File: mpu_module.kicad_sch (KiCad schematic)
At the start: 12 parts

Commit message: Eliminated all warnings realted with footprints
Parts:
- C55, C56: footprint Capacitors_Smd_0603:100nF_0603 -> Capacitors_Smd_0402:100nF_0402; symbol Capacitors_Smd0603:100n -> Capacitors_Smd0402:100nF; Developer (none) -> MW; LCSC Part # (optional) (none) -> C131394; Manufacturer SAMSUNG -> Murata; Manufacturer Part Number CL10B104JB8NNNC -> GRM155R71H104KE14D; Package 0603 -> 0402; Package_1 (none) -> 0402; Price@1000pcs 0,02231 -> 0,03299; Price@1pc 0,04540 -> 0,07091; Supplier TME -> Tme; Supplier Part Number CL10B104JB8NNNC -> GRM155R71H104KE14D; URL https://www.tme.eu/pl/details/cl10b104jb8nnnc/kondensatory-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 -> https://www.tme.eu/pl/details/grm155r71h104ke14d/kondensato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
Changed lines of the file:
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@@
     (pin "1")
   )
-  (symbol (lib_id "Capacitors_Smd0603:100n") (at 41.91 115.57 0) (unit 1)
+  (symbol (lib_id "Capacitors_Smd0402:100nF") (at 41.91 115.57 0) (unit 1)
     (in_bom yes) (on_board yes)
     (property "Reference" "C56" (id 0) (at 45.2374 114.4016 0)
@@
       (effects (font (size 1.27 1.27)) (justify left))
     )
-    (property "Footprint" "Capacitors_Smd_0603:100nF_0603" (id 2) (at 41.91 115.57 0)
-      (effects (font (size 1.524 1.524)) hide)
-    )
-    (property "Datasheet" "Capacitors/Smd_0603/Components_Documentation/KEM_C1005_Y5V_SMD.pdf" (id 3) (at 41.91 115.57 0)
-      (effects (font (size 1.524 1.524)) hide)
-    )
-    (property "Manufacturer" "SAMSUNG" (id 4) (at 41.91 115.57 0)
+    (property "Footprint" "Capacitors_Smd_0402:100nF_0402" (id 2) (at 41.91 115.57 0)
       (effects (font (size 1.27 1.27)) hide)
     )
-    (property "Manufacturer Part Number" "CL10B104JB8NNNC" (id 5) (at 41.91 115.57 0)
+    (property "Datasheet" "https://www.tme.eu/Document/558f361ed82994aff5a3e7789d970dd1/GRM155R71H104KE14-01.pdf" (id 3) (at 41.91 115.57 0)
       (effects (font (size 1.27 1.27)) hide)
     )
-    (property "Supplier" "TME" (id 6) (at 41.91 115.57 0)
+    (property "Manufacturer" "Murata" (id 4) (at 41.91 115.57 0)
       (effects (font (size 1.27 1.27)) hide)
     )
-    (property "Supplier Part Number" "CL10B104JB8NNNC" (id 7) (at 41.91 115.57 0)
+    (property "Manufacturer Part Number" "GRM155R71H104KE14D" (id 5) (at 41.91 115.57 0)
       (effects (font (size 1.27 1.27)) hide)
     )
-    (property "URL" "https://www.tme.eu/pl/details/cl10b104jb8nnnc/kondensatory-mlcc-smd-0603/samsung/" (id 8) (at 41.91 115.57 0)
+    (property "Supplier" "Tme" (id 6) (at 41.91 115.57 0)
       (effects (font (size 1.27 1.27)) hide)
     )
-    (property "Price@1pc" "0,04540" (id 9) (at 41.91 115.57 0)
+    (property "Supplier Part Number" "GRM155R71H104KE14D" (id 7) (at 41.91 115.57 0)
       (effects (font (size 1.27 1.27)) hide)
     )
-    (property "Price@1000pcs" "0,02231" (id 10) (at 41.91 115.57 0)
+    (property "URL" "https://www.tme.eu/pl/details/grm155r71h104ke14d/kondensatory-mlcc-smd-0402/murata/" (id 8) (at 41.91 115.57 0)
       (effects (font (size 1.27 1.27)) hide)
     )
-    (property "Package" "0603" (id 11) (at 41.91 115.57 0)
+    (property "Price@1pc" "0,07091" (id 9) (at 41.91 115.57 0)
+      (effects (font (size 1.27 1.27)) hide)
+    )
+    (property "Price@1000pcs" "0,03299" (id 10) (at 41.91 115.57 0)
+      (effects (font (size 1.27 1.27)) hide)
+    )
+    (property "Package" "0402" (id 11) (at 41.91 115.57 0)
+      (effects (font (size 1.27 1.27)) hide)
+    )
+    (property "Developer" "MW" (id 12) (at 41.91 115.57 0)
+      (effects (font (size 1.27 1.27)) hide)
+    )
+    (property "Package_1" "0402" (id 13) (at 41.91 115.57 0)
+      (effects (font (size 1.27 1.27)) hide)
+    )
+    (property "LCSC Part # (optional)" "C131394" (id 14) (at 41.91 115.57 0)
       (effects (font (size 1.27 1.27)) hide)
     )
@@
     (pin "1")
   )
-  (symbol (lib_id "Capacitors_Smd0603:100n") (at 29.21 115.57 0) (unit 1)
+  (symbol (lib_id "Capacitors_Smd0402:100nF") (at 29.21 115.57 0) (unit 1)
     (in_bom yes) (on_board yes)
     (property "Reference" "C55" (id 0) (at 32.5374 114.4016 0)
@@
       (effects (font (size 1.27 1.27)) (justify left))
     )
-    (property "Footprint" "Capacitors_Smd_0603:100nF_0603" (id 2) (at 29.21 115.57 0)
-      (effects (font (size 1.524 1.524)) hide)
-    )
-    (property "Datasheet" "Capacitors/Smd_0603/Components_Documentation/KEM_C1005_Y5V_SMD.pdf" (id 3) (at 29.21 115.57 0)
-      (effects (font (size 1.524 1.524)) hide)
-    )
-    (property "Manufacturer" "SAMSUNG" (id 4) (at 29.21 115.57 0)
+    (property "Footprint" "Capacitors_Smd_0402:100nF_0402" (id 2) (at 29.21 115.57 0)
       (effects (font (size 1.27 1.27)) hide)
     )
-    (property "Manufacturer Part Number" "CL10B104JB8NNNC" (id 5) (at 29.21 115.57 0)
+    (property "Datasheet" "https://www.tme.eu/Document/558f361ed82994aff5a3e7789d970dd1/GRM155R71H104KE14-01.pdf" (id 3) (at 29.21 115.57 0)
       (effects (font (size 1.27 1.27)) hide)
     )
-    (property "Supplier" "TME" (id 6) (at 29.21 115.57 0)
+    (property "Manufacturer" "Murata" (id 4) (at 29.21 115.57 0)
       (effects (font (size 1.27 1.27)) hide)
     )
-    (property "Supplier Part Number" "CL10B104JB8NNNC" (id 7) (at 29.21 115.57 0)
+    (property "Manufacturer Part Number" "GRM155R71H104KE14D" (id 5) (at 29.21 115.57 0)
       (effects (font (size 1.27 1.27)) hide)
     )
-    (property "URL" "https://www.tme.eu/pl/details/cl10b104jb8nnnc/kondensatory-mlcc-smd-0603/samsung/" (id 8) (at 29.21 115.57 0)
+    (property "Supplier" "Tme" (id 6) (at 29.21 115.57 0)
       (effects (font (size 1.27 1.27)) hide)
     )
-    (property "Price@1pc" "0,04540" (id 9) (at 29.21 115.57 0)
+    (property "Supplier Part Number" "GRM155R71H104KE14D" (id 7) (at 29.21 115.57 0)
       (effects (font (size 1.27 1.27)) hide)
     )
-    (property "Price@1000pcs" "0,02231" (id 10) (at 29.21 115.57 0)
+    (property "URL" "https://www.tme.eu/pl/details/grm155r71h104ke14d/kondensatory-mlcc-smd-0402/murata/" (id 8) (at 29.21 115.57 0)
       (effects (font (size 1.27 1.27)) hide)
     )
-    (property "Package" "0603" (id 11) (at 29.21 115.57 0)
+    (property "Price@1pc" "0,07091" (id 9) (at 29.21 115.57 0)
       (effects (font (size 1.27 1.27)) hide)
     )
+    (property "Price@1000pcs" "0,03299" (id 10) (at 29.21 115.57 0)
+      (effects (font (size 1.27 1.27)) hide)
+    )
+    (property "Package" "0402" (id 11) (at 29.21 115.57 0)
+      (effects (font (size 1.27 1.27)) hide)
+    )
+    (property "Developer" "MW" (id 12) (at 29.21 115.57 0)
+      (effects (font (size 1.27 1.27)) hide)
+    )
+    (property "Package_1" "0402" (id 13) (at 29.21 115.57 0)
+      (effects (font (size 1.27 1.27)) hide)
+    )
+    (property "LCSC Part # (optional)" "C131394" (id 14) (at 29.21 115.57 0)
+      (effects (font (size 1.27 1.27)) hide)
+    )

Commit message: Gerbers created, BOM, CPL
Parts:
- C55, C56: value 100n -> 100nF/50V
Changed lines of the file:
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@@
       (effects (font (size 1.27 1.27)) hide)
     )
-    (property "Datasheet" "Resistors/Smd_0603/Components_Documentation/Vishay_Resistors_SM0603.pdf" (id 3) (at 161.29 193.04 0)
+    (property "Datasheet" "https://www.tme.eu/Document/b315665a56acbc42df513c99b390ad98/ROYALOHM-THICKFILM.pdf" (id 3) (at 161.29 193.04 0)
       (effects (font (size 1.27 1.27)) hide)
     )
@@
       (effects (font (size 1.27 1.27)) hide)
     )
-    (property "Datasheet" "Resistors/Smd_0603/Components_Documentation/Vishay_Resistors_SM0603.pdf" (id 3) (at 144.78 130.81 0)
+    (property "Datasheet" "https://www.tme.eu/Document/b315665a56acbc42df513c99b390ad98/ROYALOHM-THICKFILM.pdf" (id 3) (at 144.78 130.81 0)
       (effects (font (size 1.27 1.27)) hide)
     )
@@
       (effects (font (size 1.524 1.524)) hide)
     )
-    (property "Datasheet" "Resistors/Smd_0603/Components_Documentation/Vishay_Resistors_SM0603.pdf" (id 3) (at 25.4 158.75 0)
+    (property "Datasheet" "https://www.tme.eu/Document/4f50d320a6ddacb273098f84373b6259/rezystor-smd.pdf" (id 3) (at 25.4 158.75 0)
       (effects (font (size 1.524 1.524)) hide)
     )
@@
       (effects (font (size 1.524 1.524)) hide)
     )
-    (property "Datasheet" "Resistors/Smd_0603/Components_Documentation/Vishay_Resistors_SM0603.pdf" (id 3) (at 33.02 158.75 0)
+    (property "Datasheet" "https://www.tme.eu/Document/4f50d320a6ddacb273098f84373b6259/rezystor-smd.pdf" (id 3) (at 33.02 158.75 0)
       (effects (font (size 1.524 1.524)) hide)
     )
@@
       (effects (font (size 1.524 1.524)) hide)
     )
-    (property "Datasheet" "Resistors/Smd_0603/Components_Documentation/Vishay_Resistors_SM0603.pdf" (id 3) (at 40.64 158.75 0)
+    (property "Datasheet" "https://www.tme.eu/Document/4f50d320a6ddacb273098f84373b6259/rezystor-smd.pdf" (id 3) (at 40.64 158.75 0)
       (effects (font (size 1.524 1.524)) hide)
     )
@@
       (effects (font (size 1.524 1.524)) hide)
     )
-    (property "Datasheet" "Resistors/Smd_0603/Components_Documentation/Vishay_Resistors_SM0603.pdf" (id 3) (at 25.4 181.61 0)
+    (property "Datasheet" "https://www.tme.eu/Document/4f50d320a6ddacb273098f84373b6259/rezystor-smd.pdf" (id 3) (at 25.4 181.61 0)
       (effects (font (size 1.524 1.524)) hide)
     )
@@
       (effects (font (size 1.524 1.524)) hide)
     )
-    (property "Datasheet" "Resistors/Smd_0603/Components_Documentation/Vishay_Resistors_SM0603.pdf" (id 3) (at 33.02 181.61 0)
+    (property "Datasheet" "https://www.tme.eu/Document/4f50d320a6ddacb273098f84373b6259/rezystor-smd.pdf" (id 3) (at 33.02 181.61 0)
       (effects (font (size 1.524 1.524)) hide)
     )
@@
       (effects (font (size 1.524 1.524)) hide)
     )
-    (property "Datasheet" "Resistors/Smd_0603/Components_Documentation/Vishay_Resistors_SM0603.pdf" (id 3) (at 40.64 181.61 0)
+    (property "Datasheet" "https://www.tme.eu/Document/4f50d320a6ddacb273098f84373b6259/rezystor-smd.pdf" (id 3) (at 40.64 181.61 0)
       (effects (font (size 1.524 1.524)) hide)
     )
@@
       (effects (font (size 1.27 1.27)) (justify left))
     )
-    (property "Value" "100n" (id 1) (at 45.2374 116.713 0)
+    (property "Value" "100nF/50V" (id 1) (at 42.545 118.11 0)
       (effects (font (size 1.27 1.27)) (justify left))
     )
@@
       (effects (font (size 1.27 1.27)) (justify left))
     )
-    (property "Value" "100n" (id 1) (at 32.5374 116.713 0)
-      (effects (font (size 1.27 1.27)) (justify left))
-    )
+    (property "Value" "100nF/50V" (id 1) (at 29.845 118.11 0)
+      (effects (font (size 1.27 1.27)) (justify left))
+    )

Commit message: New branch created
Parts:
- added R80: (no value), symbol Resistors_Smd0402:0R
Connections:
- net JTAG-~{TRST}: now also R80.1; no longer SOM1.48 (JTAG_nTRST)
- new net: R80.2, SOM1.48 (JTAG_nTRST)

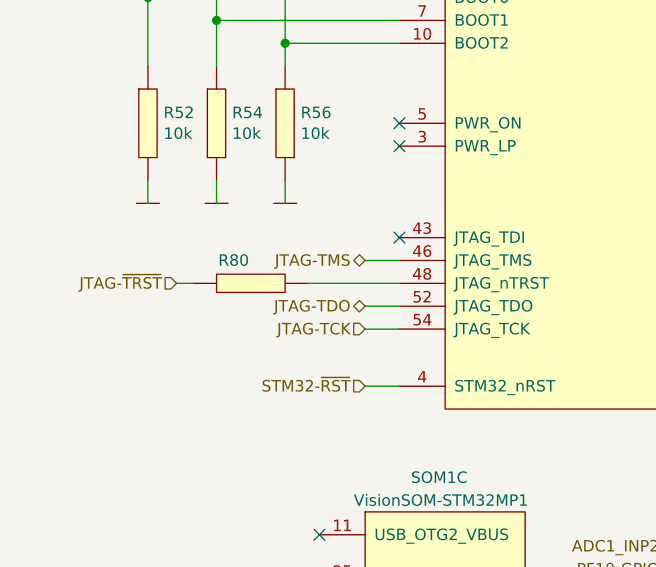
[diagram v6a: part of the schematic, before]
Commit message: Changed ethernet connector to horizontal and changed it position to avoid collision with arduino shield
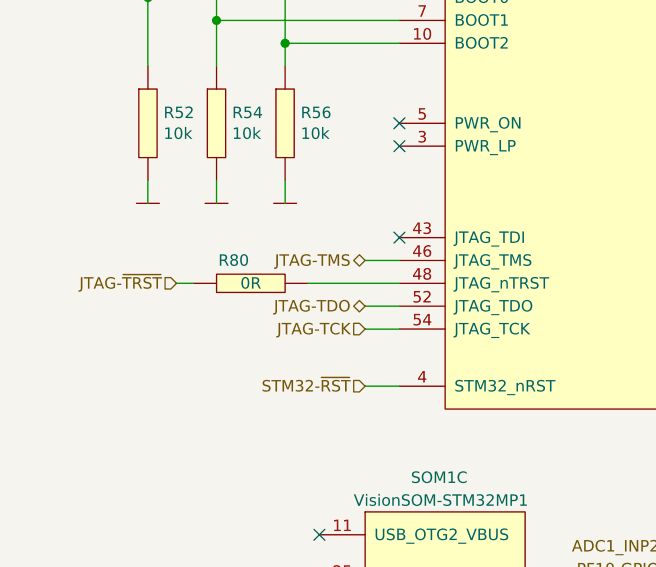
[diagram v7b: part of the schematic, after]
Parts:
- R80: value (none) -> 0R; footprint (none) -> Resistor_Smd_0402:0R_0402
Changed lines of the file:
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@@
     (in_bom yes) (on_board yes)
     (property "Reference" "R80" (id 0) (at 34.925 196.85 90))
-    (property "Value" "" (id 1) (at 36.83 199.39 90))
-    (property "Footprint" "" (id 2) (at 44.45 195.58 0)
+    (property "Value" "0R" (id 1) (at 36.83 199.39 90))
+    (property "Footprint" "Resistor_Smd_0402:0R_0402" (id 2) (at 44.45 195.58 0)
       (effects (font (size 1.27 1.27)) hide)
     )
